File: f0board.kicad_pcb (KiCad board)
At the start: 2 copper layers, 31 x 18.3 mm, 28 parts, among them P1 CONN_12, P2 CONN_12, SW1 SW_PUSH, U1 STM32F303CCT6, U2 MCP1700, U3 MAX3051, X1 XTAL-SMD-4-PADS

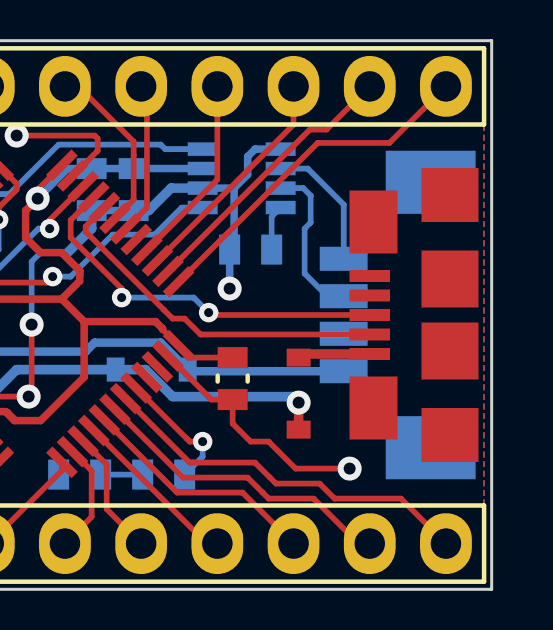
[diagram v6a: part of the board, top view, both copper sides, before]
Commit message: Connect USB shield to GND, update footprints to fix DRC issue.
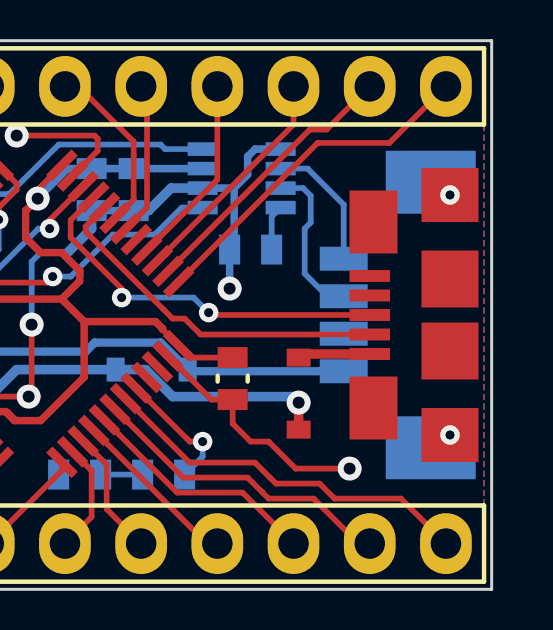
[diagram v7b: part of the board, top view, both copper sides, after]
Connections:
- CONN2 pad MECH: (no net) -> GND
- CONN3 pad 6: Net-(CONN3-Pad6) -> GND
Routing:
- net GND: vias 9 -> 11
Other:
- rule pad_to_mask_clearance: 0.13 -> 0.14

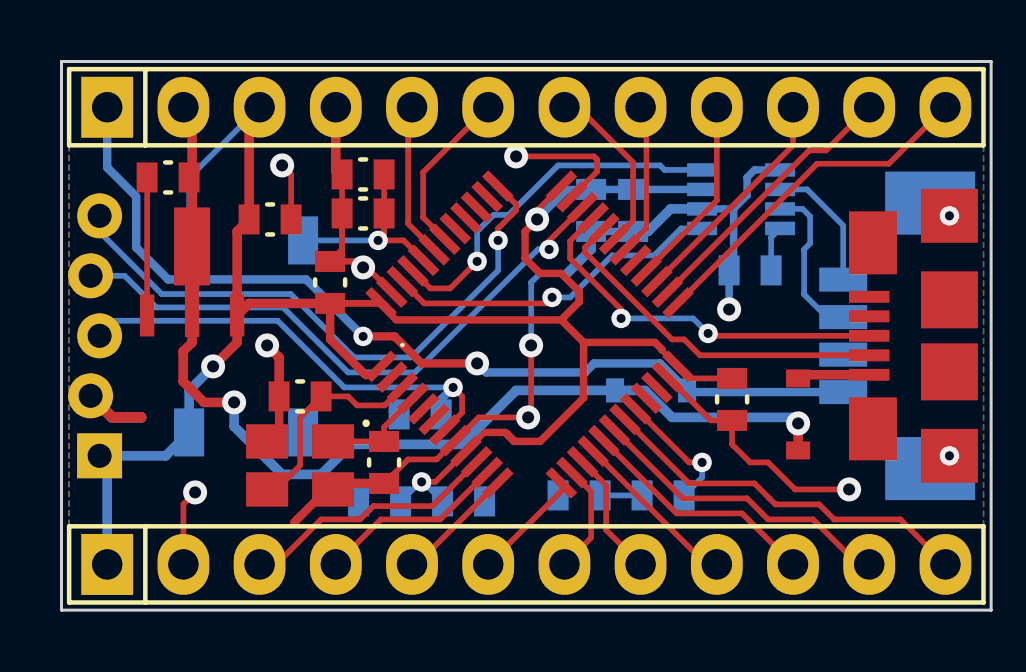
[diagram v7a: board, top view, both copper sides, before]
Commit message: Changes at Crystal after review, improved GND connection.
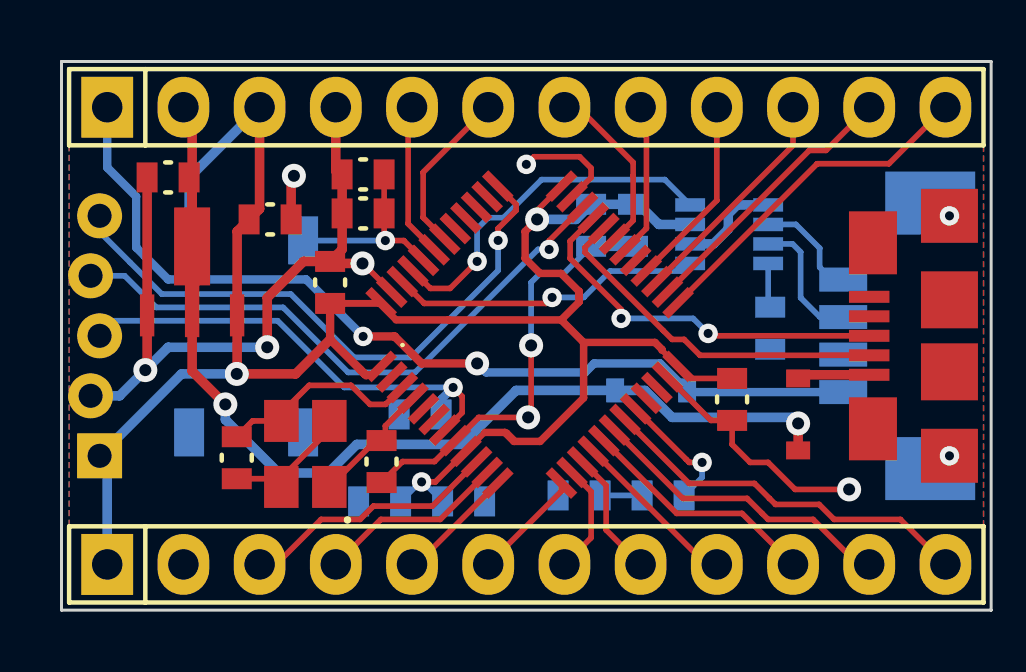
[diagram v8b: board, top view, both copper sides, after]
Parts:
- moved C10 2.94 mm to (107.2, 72.6), turned to 270 degrees
- moved R3 2.04 mm to (125.0, 68.3), turned to 270 degrees
- moved U3 1.23 mm to (122.3, 66.2)
- moved C2 0.50 mm to (120.4, 64.9)
- moved C3 0.50 mm to (119.0, 64.9)
- moved X1 0.42 mm to (109.5, 72.5), turned to 90 degrees
- moved C9 0.09 mm to (112.0, 72.8)
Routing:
- net GND: track 71.3 -> 61.2 mm, vias 11 -> 10
- net VCC: track 75.1 -> 77.7 mm
- net /CAN_TX: track 11.3 -> 10.4 mm
- net /5V: track 37.4 -> 36.6 mm
- net Net-(CONN2-Pad4): track 4.40 -> 3.63 mm
- net /BOOT0: track 7.27 -> 6.51 mm
- net Net-(C9-Pad1): track 3.54 -> 4.22 mm
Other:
- rule trace_min: 0.1524 -> 0.16
